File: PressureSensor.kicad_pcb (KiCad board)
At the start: 2 copper layers, 79.2 x 58.4 mm, 15 parts, among them U1 MPX5050DP, U2 MPX5050DP, U3 MPX5050DP

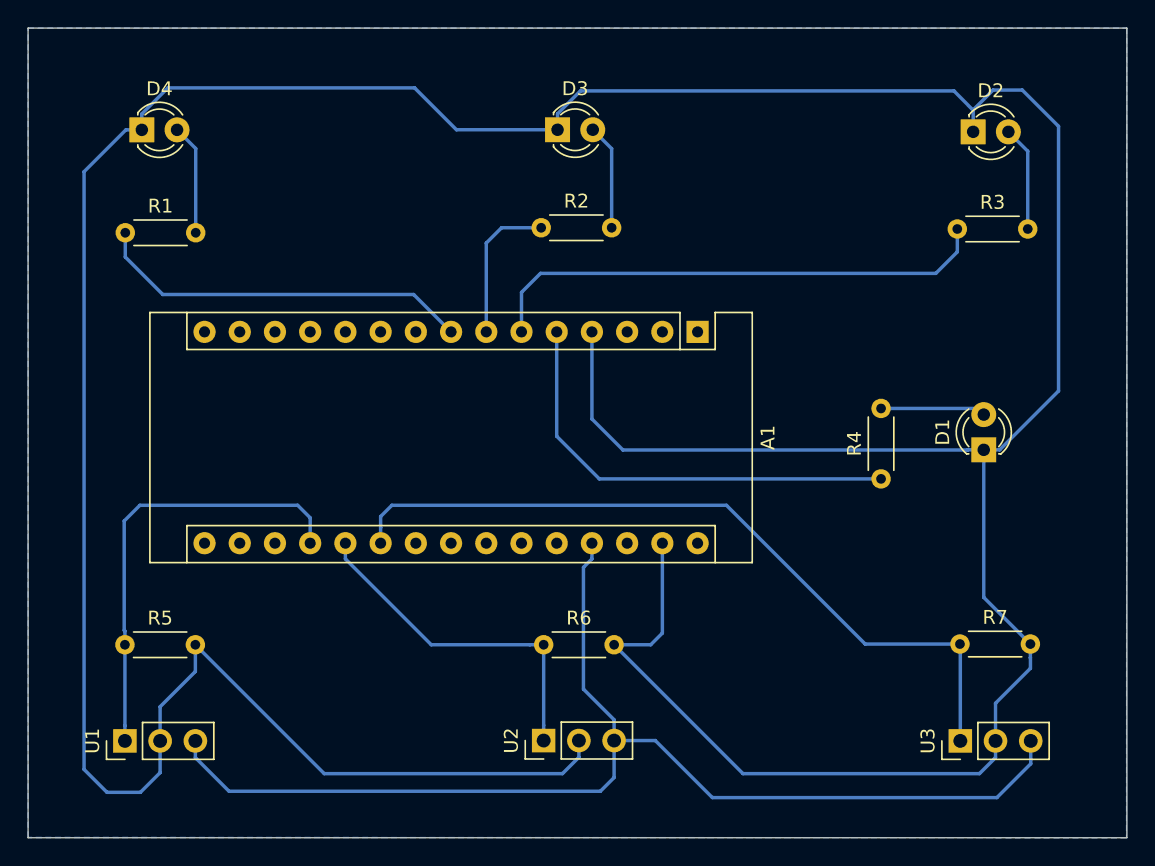
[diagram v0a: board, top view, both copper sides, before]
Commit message: Modify Track Width and Plot
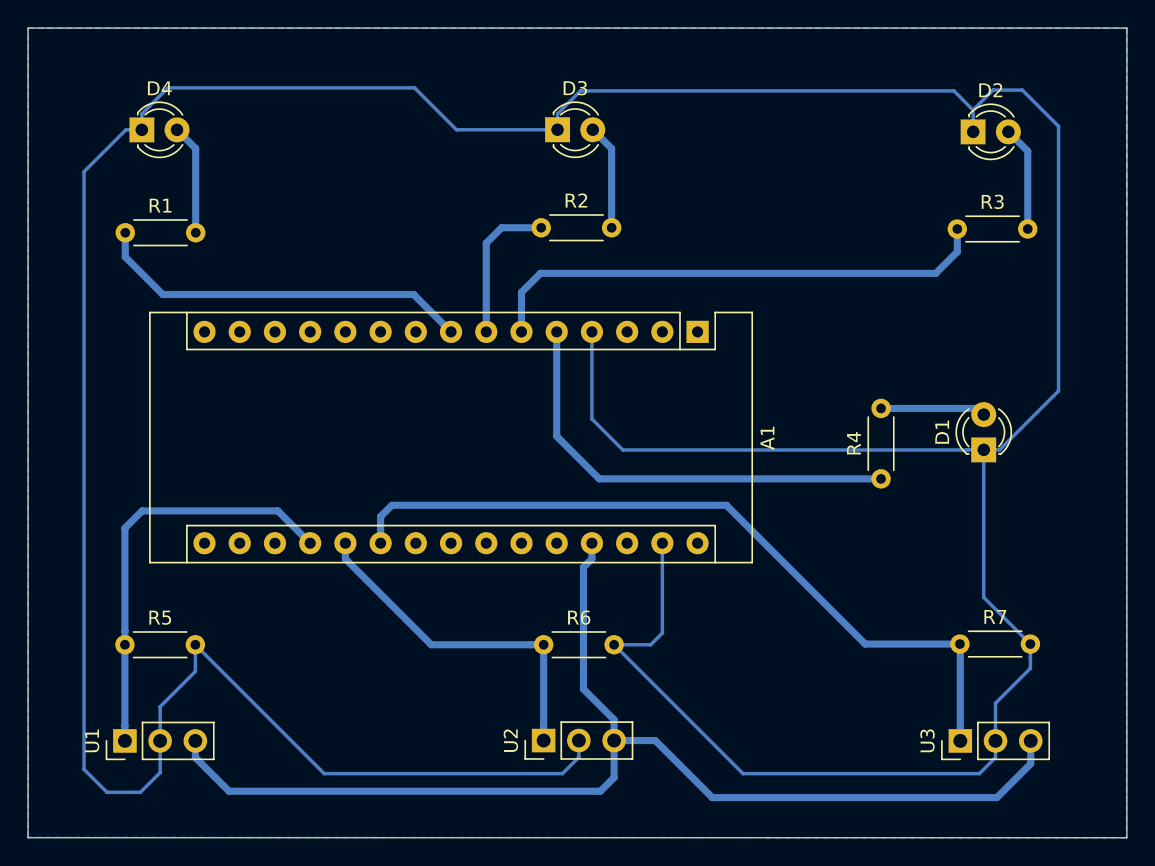
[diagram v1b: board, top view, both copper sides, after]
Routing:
- net Net-(A1-Pad19): track 32.0 -> 30.3 mm
